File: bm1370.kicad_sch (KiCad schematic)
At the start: 48 parts, among them U5 MCP1824T-1202E/OT, U6 MCP1824T-0802E, U7 25MHz, U8 BM1370_mode1, U9 SN74AVC4T774

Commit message: lots of misc
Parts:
- removed C37, C38: 0.1uF, Capacitor_SMD:C_0402_1005Metric, symbol Device:C
- removed C39, C40: 1uF, Capacitor_SMD:C_0402_1005Metric, symbol Device:C
- added C54: 100uF, Capacitor_SMD:C_1206_3216Metric, symbol Device:C
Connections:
- net GND: now also C54.2
- net VDD: now also C54.1

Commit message: layout
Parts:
- removed TP17: TestPoint, TestPoint:TestPoint_Pad_D1.5mm, symbol Connector:TestPoint
- R6: now left out of the parts list
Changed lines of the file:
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@@
 	)
 	(junction
-		(at 81.28 116.84)
-		(diameter 0)
-		(color 0 0 0 0)
-	)
-	(junction
 		(at 62.23 69.85)
 		(diameter 0.9144)
@@
 	(wire
 		(pts
-			(xy 80.01 116.84) (xy 81.28 116.84)
-		)
-		(stroke
-			(width 0)
-			(type default)
-		)
-	)
-	(wire
-		(pts
 			(xy 63.5 104.14) (xy 69.85 104.14)
 		)
@@
 		(unit 1)
 		(exclude_from_sim no)
-		(in_bom yes)
-		(on_board yes)
+		(in_bom no)
+		(on_board no)
 		(dnp yes)
 		(property "Reference" "R6"
@@
 					(unit 1)
 				)
-			)
-		)
-	)
-	(symbol
-		(lib_id "Connector:TestPoint")
-		(at 80.01 116.84 90)
-		(unit 1)
-		(exclude_from_sim no)
-		(in_bom no)
-		(on_board yes)
-		(dnp no)
-		(property "Reference" "TP17"
-			(at 73.025 116.84 90)
-			(effects
-				(font
-					(size 1.27 1.27)
-				)
-			)
-		)
-		(property "Value" "TestPoint"
-			(at 74.295 115.5701 90)
-			(effects
-				(font
-					(size 1.27 1.27)
-				)
-				(justify left)
-				(hide yes)
-			)
-		)
-		(property "Footprint" "TestPoint:TestPoint_Pad_D1.5mm"
-			(at 80.01 111.76 0)
-			(effects
-				(font
-					(size 1.27 1.27)
-				)
-				(hide yes)
-			)
-		)
-		(property "Datasheet" "~"
-			(at 80.01 111.76 0)
-			(effects
-				(font
-					(size 1.27 1.27)
-				)
-				(hide yes)
-			)
-		)
-		(property "Description" ""
-			(at 80.01 116.84 0)
-			(effects
-				(font
-					(size 1.27 1.27)
-				)
-				(hide yes)
-			)
-		)
-		(pin "1"
-		)
-		(instances
-			(project "bitaxeGamma"
-				(path "/e63e39d7-6ac0-4ffd-8aa3-1841a4541b55/4cf9c075-d009-4c35-9949-adda70ae20c7"
-					(reference "TP17")
-					(unit 1)
-				)

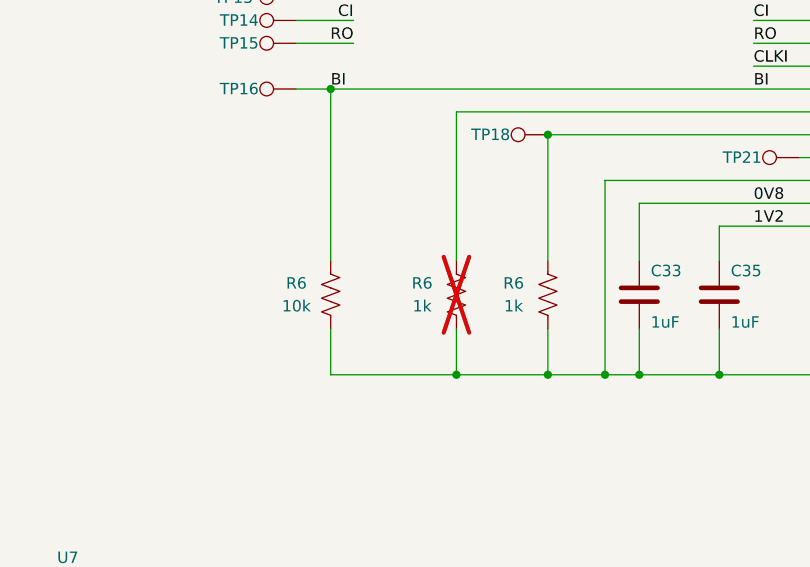
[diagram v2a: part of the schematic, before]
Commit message: added pullup resistors for #25
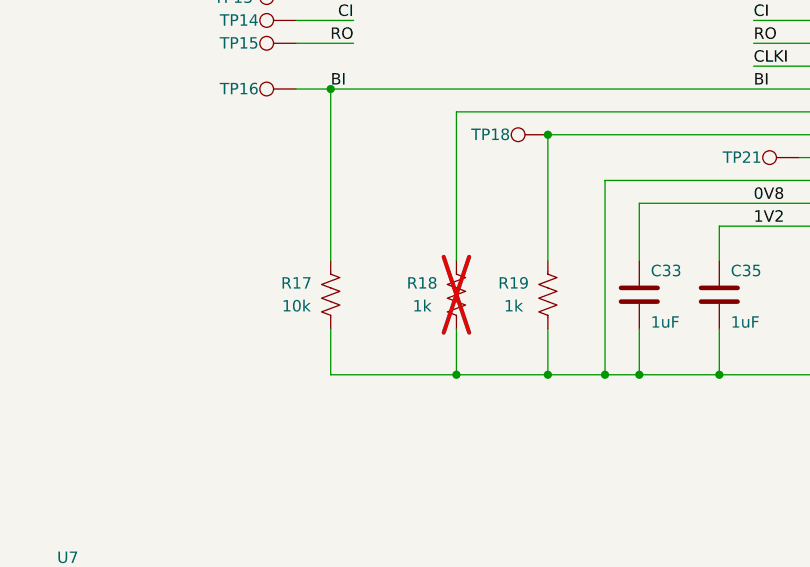
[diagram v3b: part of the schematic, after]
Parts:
- renumbered R6 to R17, R6 to R18, R6 to R19

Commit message: BOM cleanup
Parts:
- U7: DK (none) -> 5852-SX3M25.000E20F30THNTR-ND
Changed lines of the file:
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@@
 			)
 		)
-		(property "Datasheet" ""
+		(property "Datasheet" "https://www.sctf-crystal.com/data/upload/admin/20240419/3CV-Series-2024-04-19.pdf"
 			(at 40.64 172.72 0)
 			(effects
@@
 			)
 		)
-		(property "DK" ""
+		(property "DK" "5852-SX3M25.000E20F30THNTR-ND"
 			(at 41.91 171.45 0)
 			(effects
@@
 			)
 		)
-		(property "HEIGHT" ""
-			(at 41.91 171.45 0)
-			(effects
-				(font
-					(size 1.27 1.27)
-				)
-			)
-		)
-		(property "Mouser" ""
-			(at 41.91 171.45 0)
-			(effects
-				(font
-					(size 1.27 1.27)
-				)
-			)
-		)

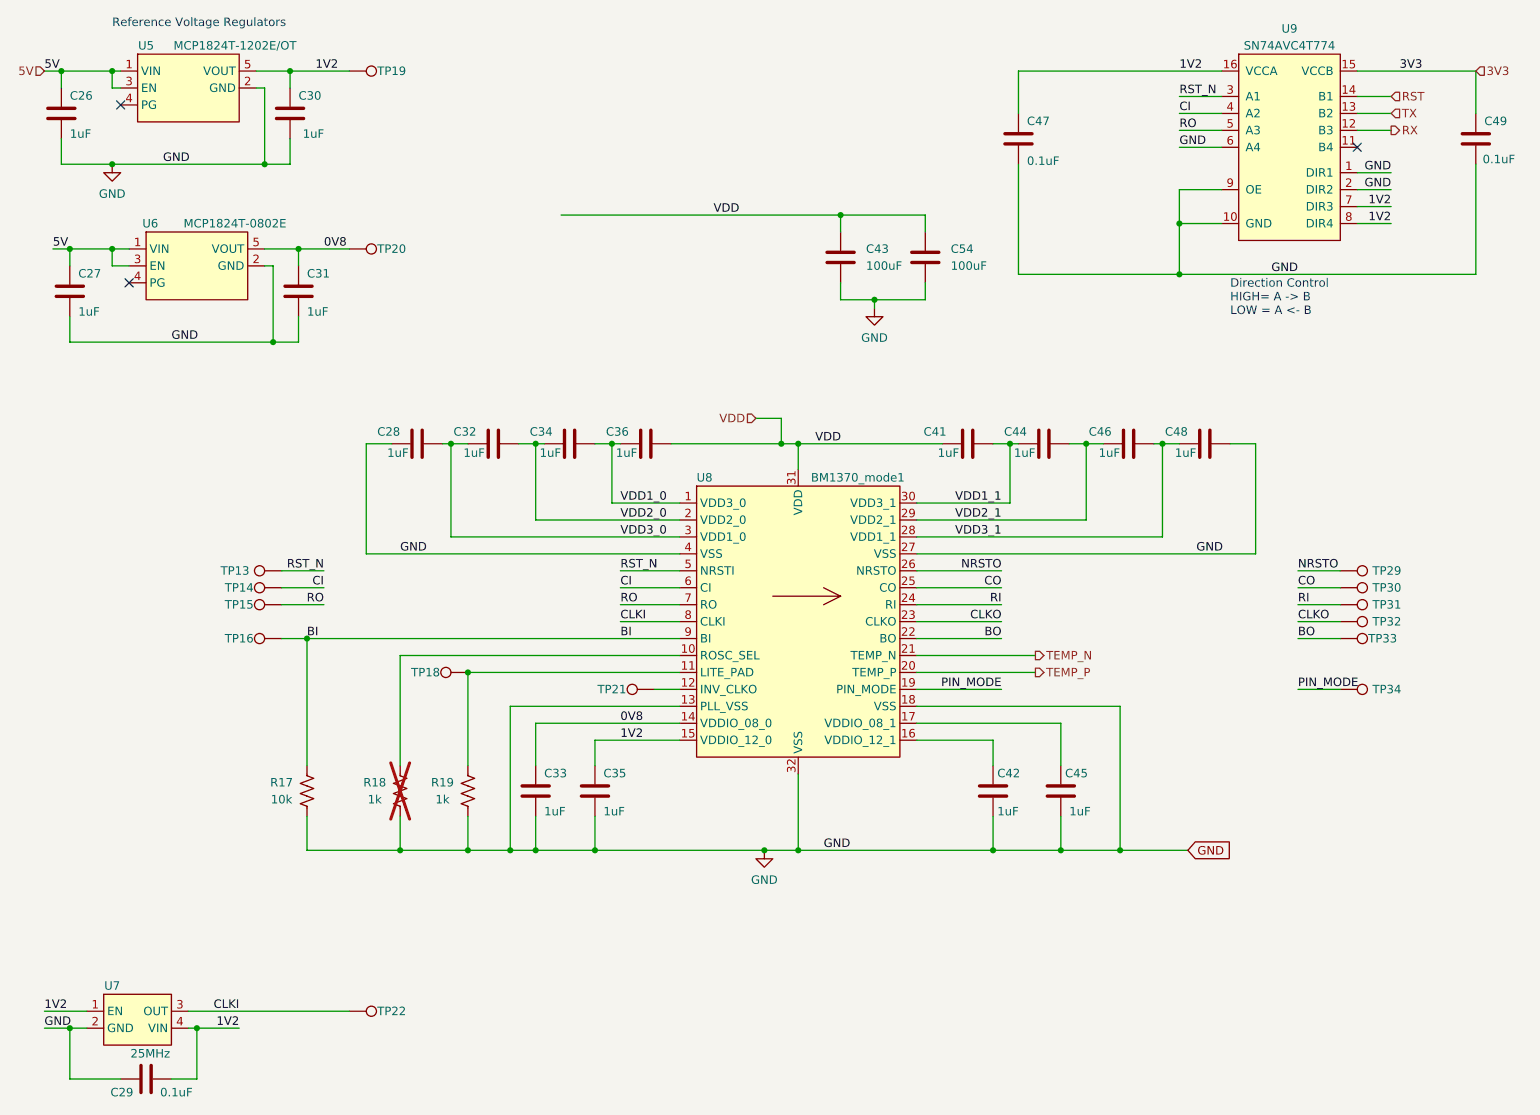
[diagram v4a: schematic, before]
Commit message: remove incorrect J3 partno for #28. removed random dust from mounting hole positions for #32. bumped version to 603. added NRSTO pulldown. added NRSTI pulldown for #36. removed old manufacturing files.
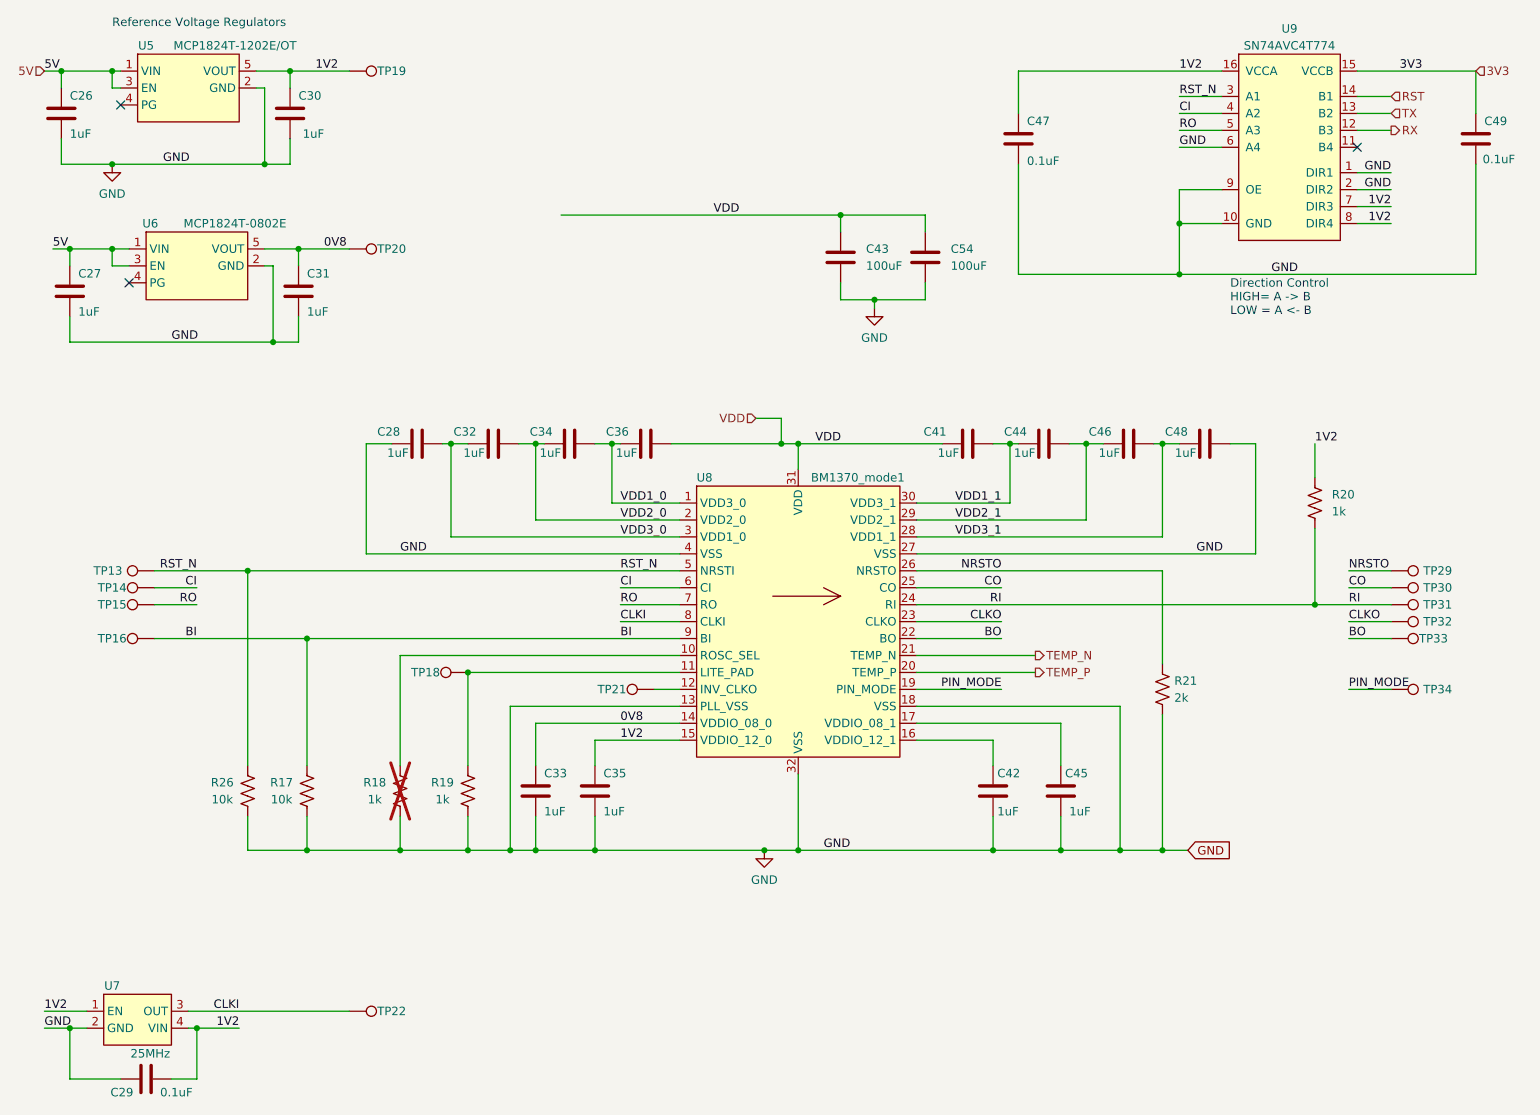
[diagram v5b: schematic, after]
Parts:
- added R20: 1k, Resistor_SMD:R_0402_1005Metric, symbol Device:R_US
- added R21: 2k, Resistor_SMD:R_0402_1005Metric, symbol Device:R_US
- added R26: 10k, Resistor_SMD:R_0402_1005Metric, symbol Device:R_US
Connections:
- net 1V2: now also R20.1
- net GND: now also R21.2, R26.1
- net NRSTO: now also R21.1
- net RI: now also R20.2
- net RST_N: now also R26.2
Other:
- moved on the sheet: TP13, TP14, TP15, TP16, TP29, TP30, TP31, TP32, TP33, TP34

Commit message: update worksheet
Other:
- company: (none) -> bitaxeorg
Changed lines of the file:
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@@
 		(date "2025-04-29")
 		(rev "603")
+		(company "bitaxeorg")
+		(comment 1 "OHLv2")
 	)
 	(text "Reference Voltage Regulators"
